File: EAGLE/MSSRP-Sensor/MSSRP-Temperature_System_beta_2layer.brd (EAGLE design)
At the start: 100 x 100 mm, 175 parts, among them J1 POWER_JACKPTH, J10 BNCPTH, J11 BNCPTH, J2 USBSMD, J4 TE-2-TERMBLOCK, J5 TE-2-TERMBLOCK, J6 TE-2-TERMBLOCK, J7 TE-2-TERMBLOCK, J8 BNCPTH, J9 BNCPTH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

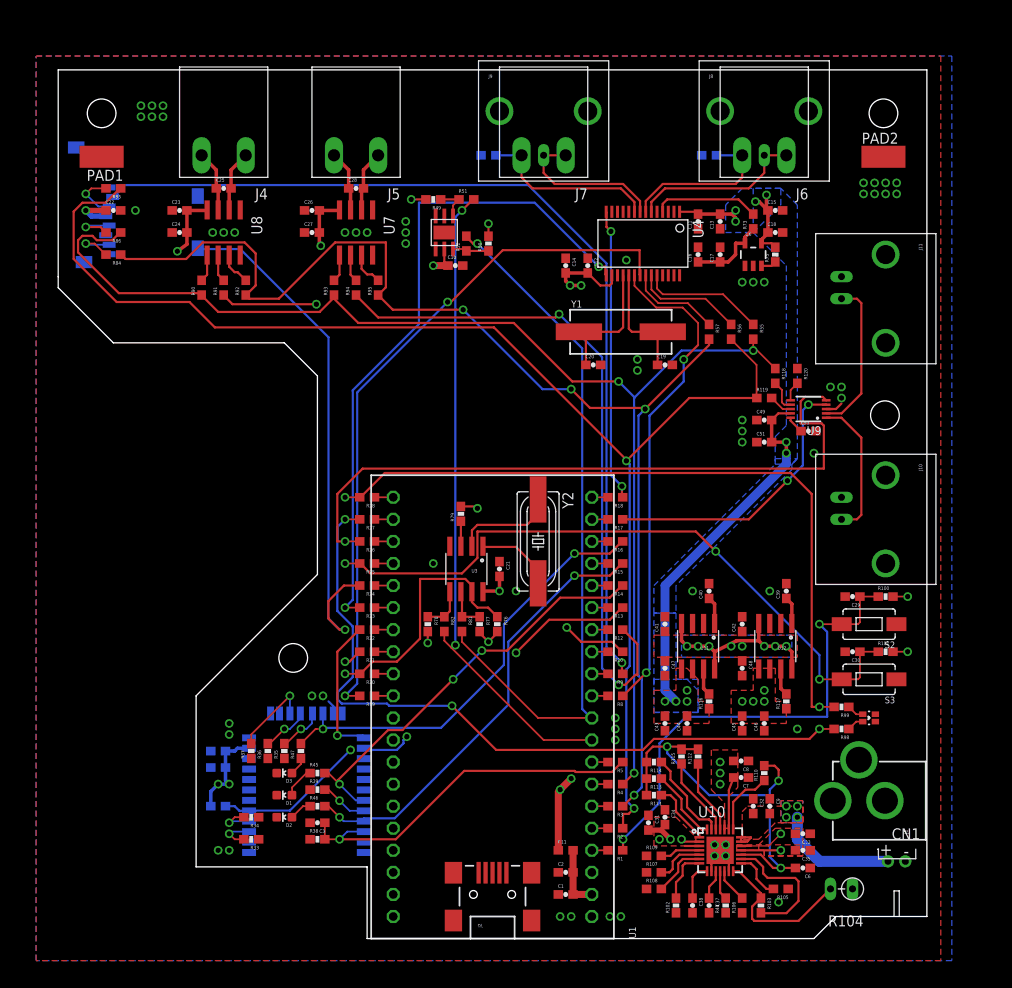
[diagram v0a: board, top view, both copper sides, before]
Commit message: Routing Update - 2-layer
Finished 4-layer route. Added 2-layer routing attempt for cost savings.
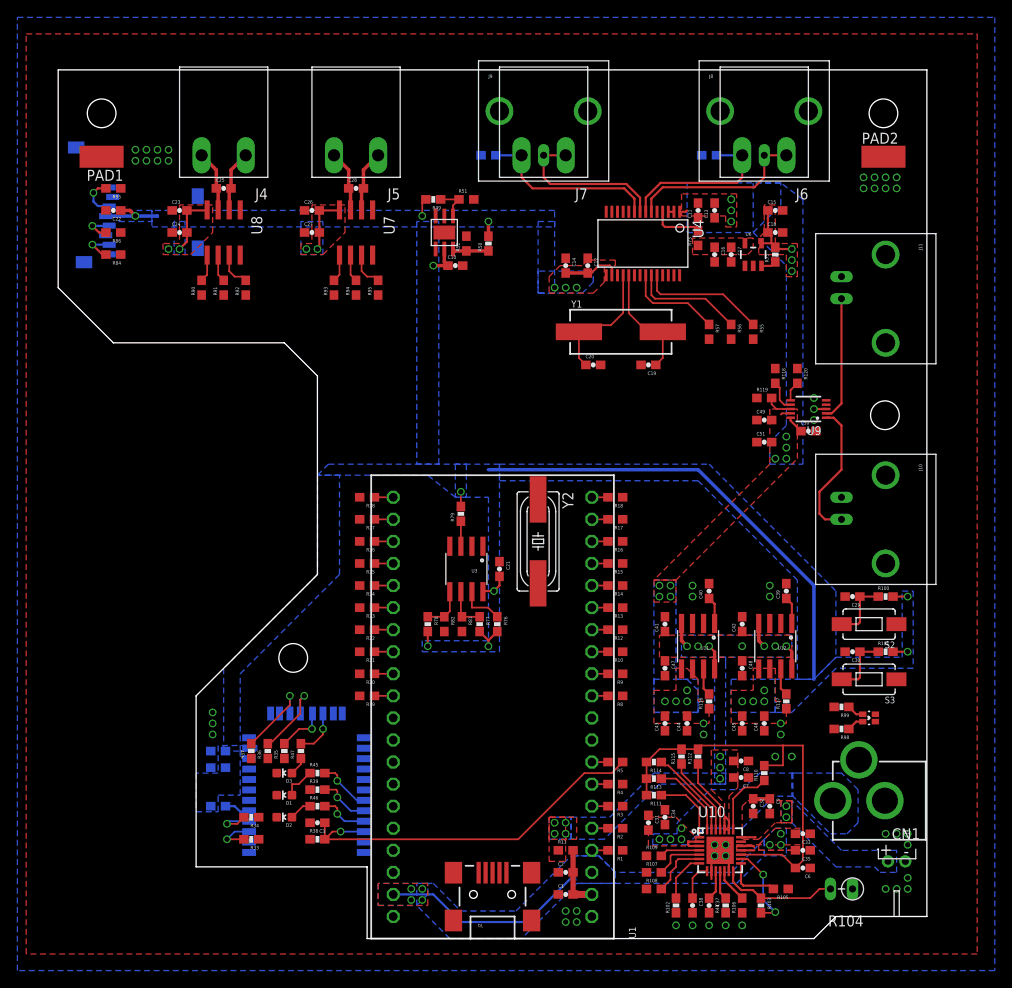
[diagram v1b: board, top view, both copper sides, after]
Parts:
- moved R73 6.63 mm to (73.7, 80.6)
- moved C16 1.91 mm to (75.6, 78.7), turned to 270 degrees
- moved C19 1.91 mm to (67.9, 66.0), turned to 180 degrees
- moved C13 1.42 mm to (75.6, 83.8)
- moved C11 1.27 mm to (73.7, 83.8)
- moved C17 1.27 mm to (77.5, 78.7), turned to 270 degrees
- turned C22 to 180 degrees
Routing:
- net MOSI: track 155.2 -> 0.00 mm, vias 2 -> 0
- net SCK: track 146.0 -> 0.00 mm, vias 3 -> 0
- net MISO: track 142.4 -> 0.00 mm, vias 4 -> 0
- net CS_SD: track 109.7 -> 0.00 mm, vias 1 -> 0
- net LED0: track 84.8 -> 0.00 mm, vias 3 -> 0
- net LED1: track 83.0 -> 0.00 mm, vias 2 -> 0
- net SCL: track 81.6 -> 0.00 mm, vias 1 -> 0
- net AFE_!DRDY: track 79.4 -> 0.00 mm, vias 2 -> 0
- net DAC_!CLR: track 78.8 -> 0.00 mm, vias 1 -> 0
- net CS_TC1: track 78.7 -> 0.00 mm, vias 2 -> 0
- net AFE_!RESET: track 77.4 -> 0.00 mm, vias 2 -> 0
- net SDA: track 75.6 -> 0.00 mm, vias 2 -> 0
- net SW2: track 77.4 -> 7.25 mm, vias 3 -> 0
- net CS_TC0: track 67.9 -> 0.00 mm, vias 2 -> 0
- net SD_CD: track 63.0 -> 0.00 mm, vias 1 -> 0
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- added copper zone on layer 16, net 3.3V
- added copper zone on layer 16, net N$6
- added copper zone on layer 16, net VIN
- added copper zone on layer 1, net VREF_2V5
- added copper zone on layer 16, net VUSB
- removed copper zone on layer 15, net 3.3V
- removed copper zone on layer 2, net GND
- removed copper zone on layer 2, net VIN
- removed copper zone on layer 2, net VSYS
- removed copper zone on layer 2, net VUSB
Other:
- outline, holes or cut-outs redrawn

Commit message: 2-layer routing
Finished 2-layer routing tasks
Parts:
- removed R10, R2, R3, R4, R8, R9: 0, SparkFun-Resistors:0603
- moved STANDOFF3 46.8 mm to (5.00, 73.6)
- moved R12 11.4 mm to (52.7, 36.2), turned to 270 degrees
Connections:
- removed net N$10: R9.2, U1.12
- removed net N$11: R10.2, U1.13
- removed net N$3: R3.2, U1.6
- removed net N$4: R4.2, U1.7
- removed net N$9: R8.2, U1.11
- net AFE_!DRDY: now also R15.1; no longer R19.2
- net AFE_!RESET: now also R17.1; no longer R23.2
- net BT_!RESET: no longer R5.1
- net BT_CONN: now also R23.2; no longer R14.1
- net BT_RESET: now also R19.2; no longer R13.1
- net BT_RXTX: now also R24.2; no longer R16.1
- net BT_STATE: now also R20.2; no longer R15.1
- net CS_AFE: now also R16.1; no longer R8.1
- net CS_SD: now also R25.2; no longer R9.1
- net CS_TC0: now also R27.2; no longer R10.1
- net CS_TC1: now also R28.2; no longer R12.1
- net DAC_!CLR: now also R14.1; no longer R26.2
- net DAC_!LDAC: now also R13.1; no longer R17.1
- net LED0: now also U1.11; no longer R27.2
- net LED1: now also U1.12; no longer R28.2
- net MISO: now also U1.6; no longer R3.1
- net MOSI: now also U1.5; no longer R2.1
- net N$2: now also R5.1; no longer R2.2, U1.5
- net RTC_SQW: now also R12.1; no longer R20.2
- net SCK: now also U1.7; no longer R4.1
- net SD_CD: now also R26.2; no longer R24.2
- net SW2: now also U1.13; no longer R25.2
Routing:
- net MOSI: track 0.00 -> 146.7 mm, vias 0 -> 5
- net MISO: track 0.00 -> 142.3 mm, vias 0 -> 3
- net SCK: track 0.00 -> 139.2 mm, vias 0 -> 1
- net SCL: track 0.00 -> 90.6 mm, vias 0 -> 3
- net SDA: track 0.00 -> 86.8 mm, vias 0 -> 3
- net MICRO_!RESET: track 7.25 -> 89.1 mm
- net CS_SD: track 0.00 -> 67.0 mm, vias 0 -> 3
- net SD_CD: track 0.00 -> 55.3 mm, vias 0 -> 1
- net LED0: track 0.00 -> 55.3 mm, vias 0 -> 1
- net LED1: track 0.00 -> 50.9 mm, vias 0 -> 1
- net SW2: track 7.25 -> 53.8 mm, vias 0 -> 1
- net DAC_!LDAC: track 0.00 -> 44.3 mm, vias 0 -> 2
- net AFE_!DRDY: track 0.00 -> 43.9 mm, vias 0 -> 2
- net AFE_!PWDN: track 0.00 -> 43.1 mm, vias 0 -> 2
- net CS_AFE: track 0.00 -> 42.6 mm, vias 0 -> 2
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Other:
- outline, holes or cut-outs redrawn

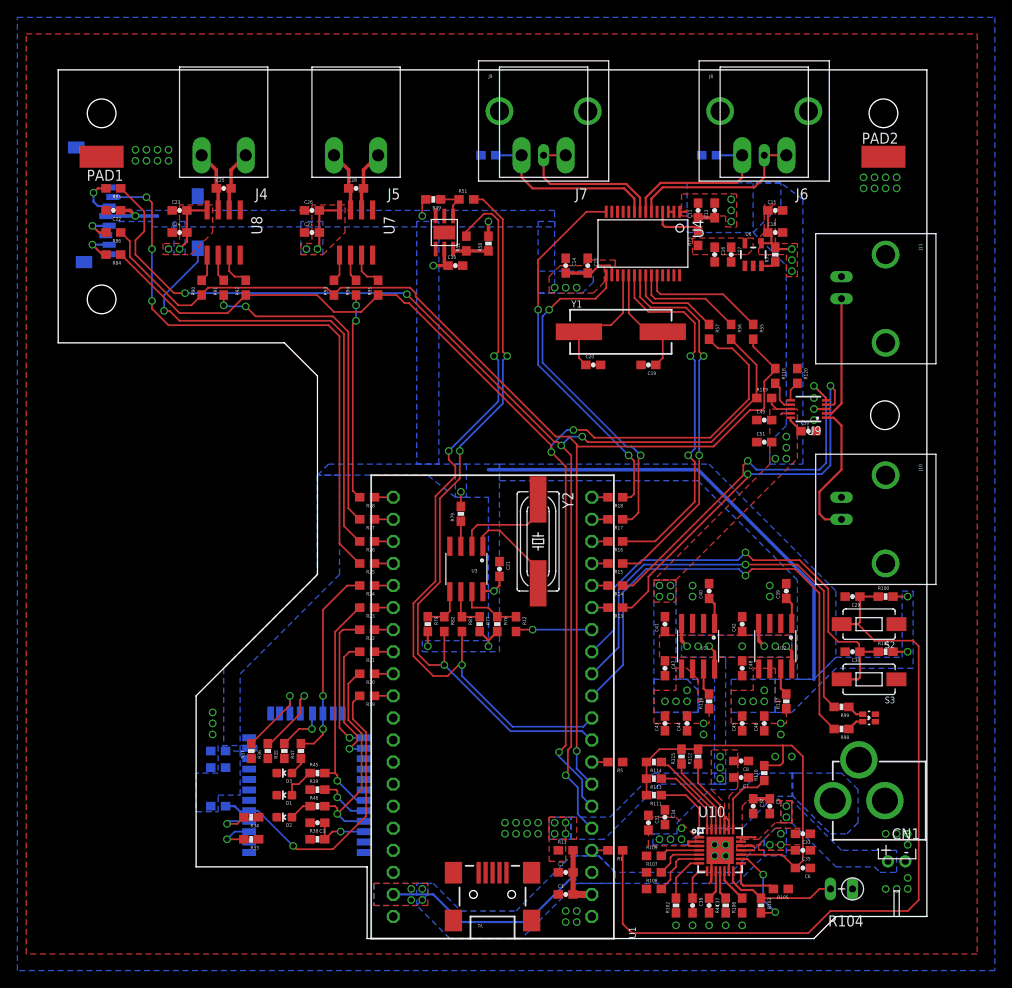
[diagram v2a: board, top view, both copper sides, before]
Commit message: Final Beta
Finished schematic checks and routing adjustments. Boards ready for
initial CAM.
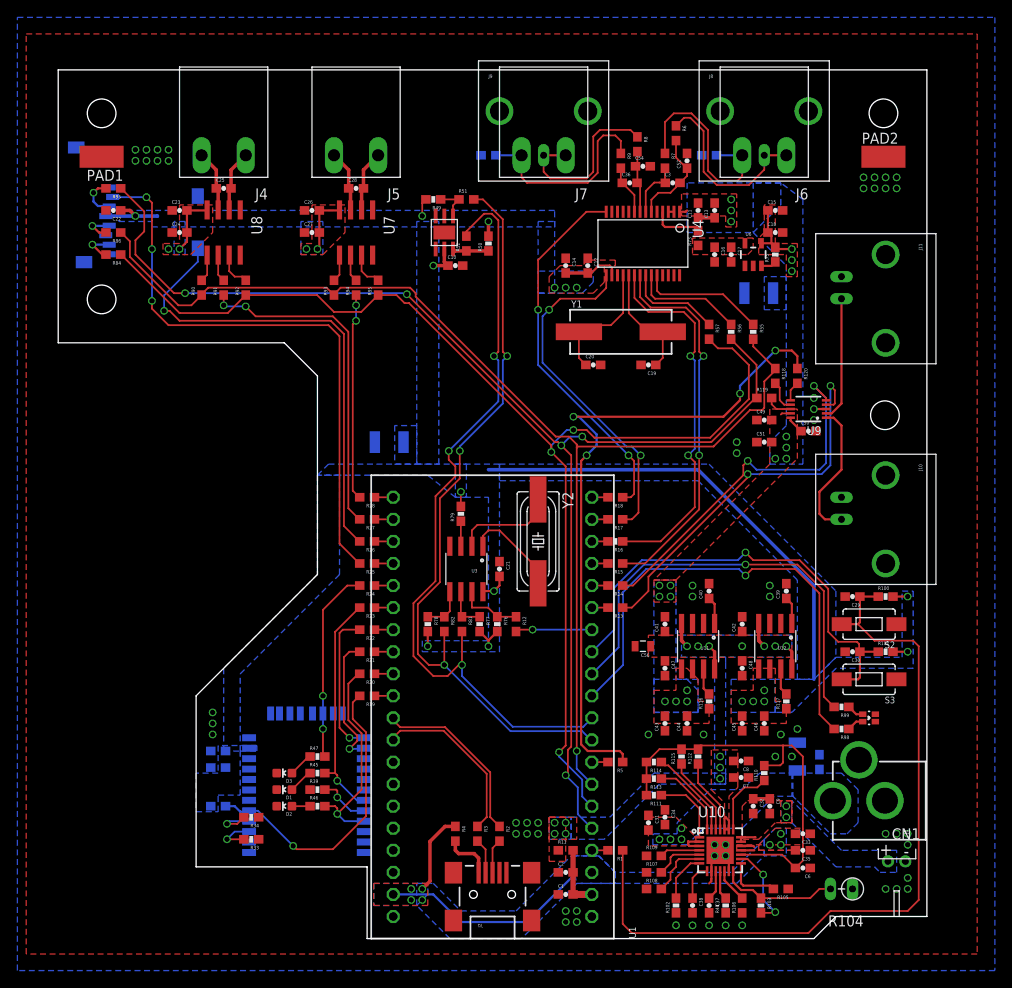
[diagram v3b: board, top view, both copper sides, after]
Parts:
- removed R35, R36, R37, R38: 10K, SparkFun-Resistors:0603-RES
- added C36, C52, C54: 10nF, SparkFun-Capacitors:0603-CAP
- added C53, C55: 47uF, SparkFun-Capacitors:EIA3528
- added C56: 22uF, SparkFun-Capacitors:0805
- added C57: 22uF, SparkFun-Capacitors:1210
- added C58: 1.0uF, SparkFun-Capacitors:0603-CAP
- added R2, R3, R4: 0, SparkFun-Resistors:0603
- added R6, R7, R8, R9: 33OHM, SparkFun-Resistors:0603
- C3: value 0.1uF -> 10nF
- C33, C8: value 4.7uF -> 10uF
- R16, R55, R56: value 0 -> 100; device SparkFun-Resistors:0603 -> SparkFun-Resistors:0603-RES
- R45, R46, R47: value 390 -> 68
- R98, R99: value 470 -> 68
- moved C3 84.3 mm to (70.7, 87.0), turned to 0 degrees
- moved R47 2.01 mm to (29.8, 21.0), turned to 0 degrees
- moved D2 1.27 mm to (26.0, 15.2)
- moved D1 0.63 mm to (26.0, 17.1)
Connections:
- removed net BT_!RESET: C3.1, R38.2, U2.22
- removed net N$35: R35.2, U2.32
- removed net N$36: R36.2, U2.33
- removed net N$37: R37.2, U2.34
- removed net UART_CTS: U2.16
- removed net UART_RTS: U2.15
- new net N$10: C36.2, C54.1, R8.2, U4.8
- new net N$11: C36.1, R9.2, U4.9
- new net N$3: J2.D+, R2.2
- new net N$4: J2.VBUS, R4.2
- new net N$7: C3.1, R7.2, U4.7
- new net N$9: C3.2, C52.1, R6.2, U4.6
- new net USB_N: R3.1, U1.32
- new net USB_P: R2.1, U1.31
- net 3.3V: now also C53.A
- net 5V: now also C55.A
- net AFE_AIN0: now also R6.1; no longer U4.6
- net AFE_AIN1: now also R7.1; no longer U4.7
- net AFE_AIN2: now also R8.1; no longer U4.8
- net AFE_AIN3: now also R9.1; no longer U4.9
- net CS_DAC: now also R5.1
- net GND: now also C52.2, C53.C, C54.2, C55.C, C56.2, C57.2, C58.2; no longer C3.2, R35.1, R36.1, R37.1, R38.1
- net N$2: now also J2.D-, R3.2; no longer R5.1
- net VIN: now also C57.1, C58.1
- net VSYS: now also C56.1
- net VUSB: now also R4.1
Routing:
- net CS_DAC: track 0.00 -> 77.7 mm, vias 0 -> 4
- net USB_P: track 0.00 -> 20.6 mm
- net USB_N: track 0.00 -> 19.9 mm
- net N$9: track 0.00 -> 11.7 mm
- net N$36: track 9.66 -> 0.00 mm, vias 1 -> 0
- net VUSB: track 27.8 -> 37.2 mm
- net N$37: track 9.37 -> 0.00 mm, vias 1 -> 0
- net N$10: track 0.00 -> 7.26 mm
- net BT_!RESET: track 6.76 -> 0.00 mm, vias 1 -> 0
- net N$7: track 0.00 -> 6.75 mm
- net N$4: track 0.00 -> 5.79 mm
- net N$35: track 5.68 -> 0.00 mm, vias 1 -> 0
- net N$11: track 0.00 -> 5.67 mm
- net AFE_AIN1: track 19.2 -> 24.5 mm, vias 0 -> 1
- net N$2: track 0.00 -> 4.02 mm
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
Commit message: DRC and Power pin
Adjustments to pass DRC: miscellaneous clearance issues and
double-drill issue with dual connector footprint.

Also added pin header connection (JP1) to VSYS as a battery system
bypass option for testing.
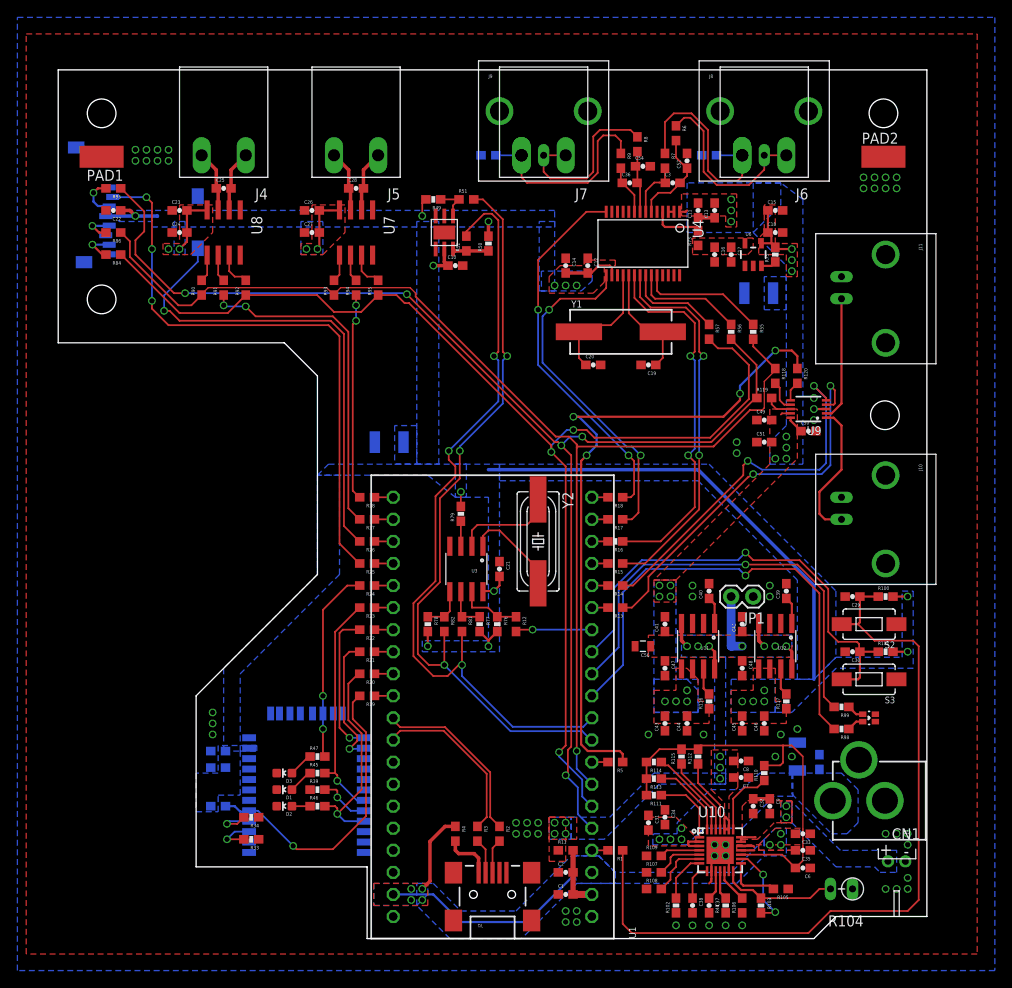
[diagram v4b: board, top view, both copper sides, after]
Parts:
- added JP1: M02PTH, SparkFun-Connectors:1X02
- J8, J9: value BNCPTH -> BNC_CUSTOM; device SparkFun-Connectors:BNC -> MSSRP-Lib:BNC_CUSTOM
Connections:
- net GND: now also JP1.1
- net VSYS: now also JP1.2
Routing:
- net VSYS: track 15.2 -> 22.1 mm
- net AFE_AIN1: vias 1 -> 0
- removed copper zone on layer 16, net N$6
